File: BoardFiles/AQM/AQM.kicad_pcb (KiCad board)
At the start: 4 copper layers, 50.4 x 50.4 mm, 40 parts, among them J1 Conn_01x04, J2 Conn_01x04, J3 Conn_01x04, J4 Conn_01x04, J5 Conn_01x04, U1 KB2040

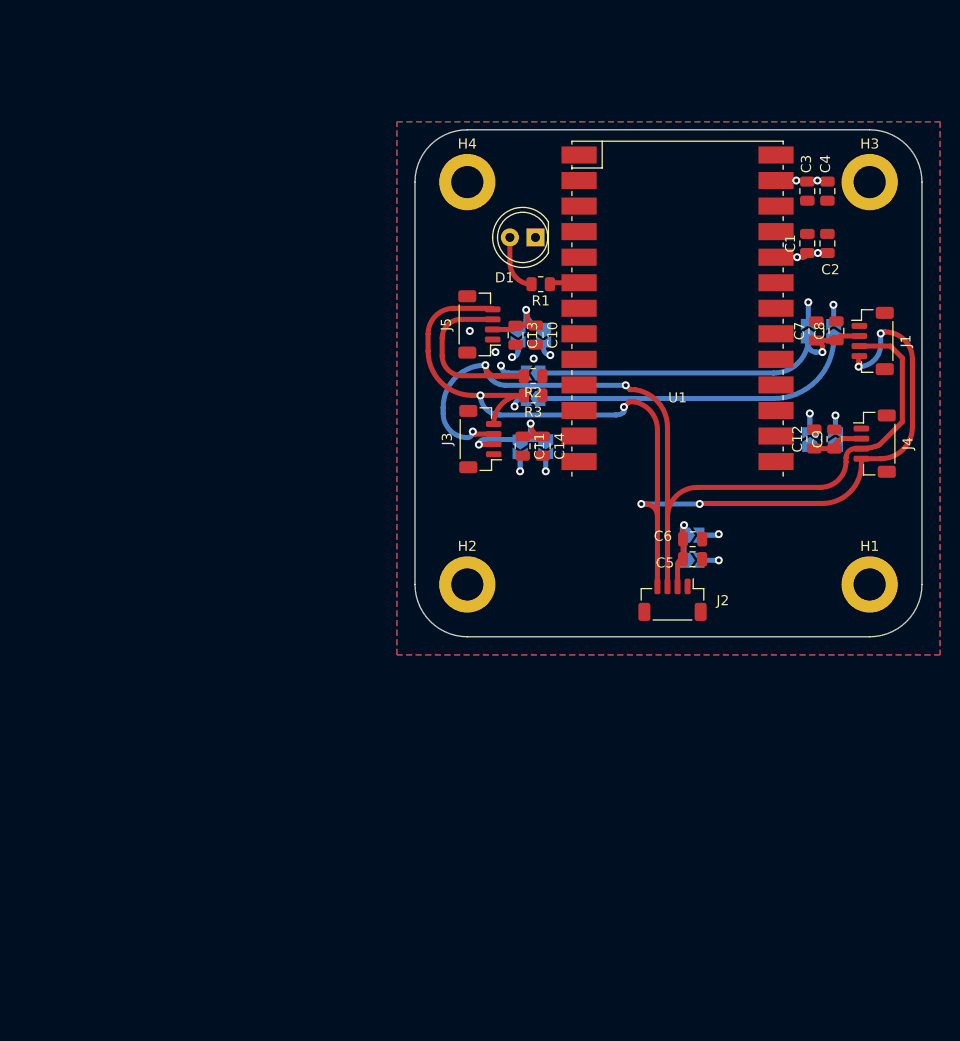
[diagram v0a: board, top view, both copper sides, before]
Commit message: Redid copper to make it look pretty
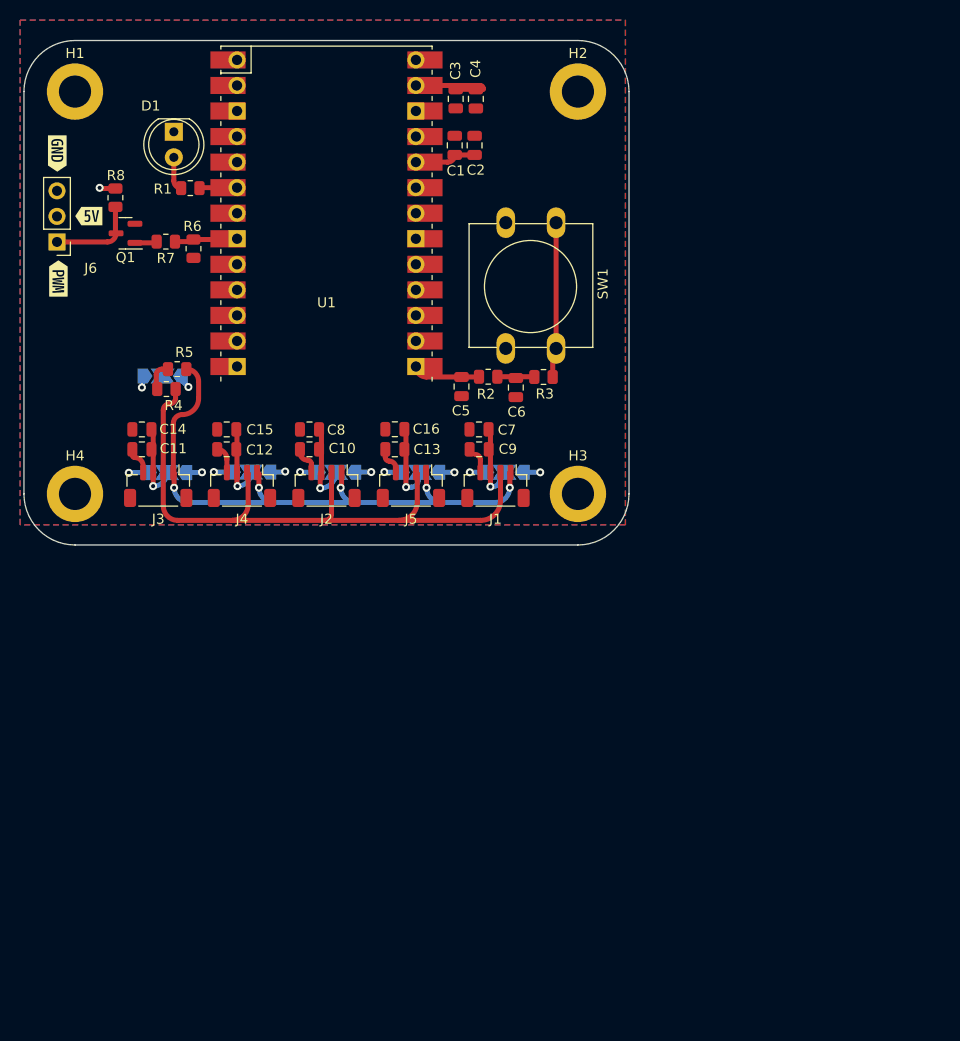
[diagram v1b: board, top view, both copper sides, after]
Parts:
- removed JP10, JP11, JP12, JP7, JP8, JP9: Jumper_2_Open, Jumper:SolderJumper-2_P1.3mm_Open_TrianglePad1.0x1.5mm
- added C15: 10u, Capacitor_SMD:C_0805_2012Metric, F.Cu at (110.1, 78.6)
- added C16: 10u, Capacitor_SMD:C_0805_2012Metric, F.Cu at (126.8, 78.6)
- added J6: Conn_01x03, Connector_PinHeader_2.54mm:PinHeader_1x03_P2.54mm_Vertical, F.Cu at (93.2, 60.0)
- added Q1: BSS138, Package_TO_SOT_SMD:SOT-23, F.Cu at (100.0, 59.1)
- added R4: 4.7K, Resistor_SMD:R_0805_2012Metric, F.Cu at (104.1, 74.6)
- added R5: 4.7K, Resistor_SMD:R_0805_2012Metric, F.Cu at (105.2, 72.6)
- added R6: 1k, Resistor_SMD:R_0805_2012Metric, F.Cu at (106.8, 60.6)
- added R7: 1k, Resistor_SMD:R_0805_2012Metric, F.Cu at (104.0, 59.9)
- added R8: 1k, Resistor_SMD:R_0805_2012Metric, F.Cu at (99.0, 55.5)
- added SW1: SW_Push, Button_Switch_THT:SW_PUSH-12mm, F.Cu at (142.8, 58.0)
- added kibuzzard-6378EB76: G***, kibuzzard-6378EB76, B.Cu at (110.3, 85.7)
- added kibuzzard-6378EB76: G***, kibuzzard-6378EB76, B.Cu at (127.1, 85.7)
- added kibuzzard-6378EB76: G***, kibuzzard-6378EB76, B.Cu at (118.7, 85.8)
- added kibuzzard-6378EB76: G***, kibuzzard-6378EB76, B.Cu at (102.0, 85.8)
- added kibuzzard-6378EB76: G***, kibuzzard-6378EB76, B.Cu at (135.4, 85.8)
- added kibuzzard-6378EBEC: G***, kibuzzard-6378EBEC, B.Cu at (139.7, 85.8)
- added kibuzzard-6378EBEC: G***, kibuzzard-6378EBEC, B.Cu at (114.6, 85.7)
- added kibuzzard-6378EBEC: G***, kibuzzard-6378EBEC, B.Cu at (122.9, 85.7)
- added kibuzzard-6378EBEC: G***, kibuzzard-6378EBEC, B.Cu at (131.4, 85.7)
- added kibuzzard-6378EBEC: G***, kibuzzard-6378EBEC, B.Cu at (106.1, 85.7)
- added kibuzzard-6378ECA4: G***, kibuzzard-6378ECA4, B.Cu at (101.5, 70.3)
- added kibuzzard-6378F2C3: G***, kibuzzard-6378F2C3, F.Cu at (93.3, 63.6)
- added kibuzzard-6378F2ED: G***, kibuzzard-6378F2ED, F.Cu at (93.2, 51.2)
- added kibuzzard-6378F316: G***, kibuzzard-6378F316, F.Cu at (96.4, 57.4)
- added kibuzzard-6378F9DB: G***, kibuzzard-6378F9DB, B.Cu at (105.6, 70.3)
- C12, C13, C6: value 10u -> 1u
- C7: value 1u -> 10u
- JP1, JP2, JP3, JP4, JP5, JP6: value Jumper_2_Open -> SolderJumper_3_Open; footprint Jumper:SolderJumper-2_P1.3mm_Open_TrianglePad1.0x1.5mm -> Jumper:SolderJumper-3_P2.0mm_Open_TrianglePad1.0x1.5mm_NumberLabels
- R2, R3: value 4.7K -> 10k
- moved H1 93.0 mm to (95.0, 45.0)
- moved J4 63.0 mm to (111.6, 84.2), turned to 180 degrees
- moved C12 58.4 mm to (110.1, 80.6), turned to 180 degrees
- moved JP3 55.0 mm to (103.7, 73.3), turned to 180 degrees
- moved C8 53.3 mm to (118.3, 78.6), turned to 180 degrees
- moved JP4 52.9 mm to (104.2, 82.9)
- moved H2 50.2 mm to (145.0, 45.0)
- moved H4 49.8 mm to (95.0, 85.0)
- moved H3 42.4 mm to (145.0, 85.0)
- moved J1 40.2 mm to (136.8, 84.2), turned to 180 degrees
- moved C14 39.9 mm to (101.7, 78.6), turned to 180 degrees
- moved C11 37.9 mm to (101.7, 80.6), turned to 180 degrees
- moved D1 37.5 mm to (104.8, 49.0), turned to -90 degrees
- moved C2 36.4 mm to (134.7, 50.4)
- moved C1 36.4 mm to (132.8, 50.4)
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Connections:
- C13 pad 1: Net-(C10-Pad1) -> Net-(C13-Pad1)
- C5 pad 1: Net-(C5-Pad1) -> Net-(U1-Pad14)
- C6 pad 1: Net-(C5-Pad1) -> Net-(C6-Pad1)
- C8 pad 1: Net-(C7-Pad1) -> Net-(C10-Pad1)
- C9 pad 1: Net-(C12-Pad1) -> Net-(C7-Pad1)
- J1 pad 1: GND -> /I2C/I2C.SCL
- J1 pad 2: Net-(C7-Pad1) -> /I2C/I2C.SDA
- J1 pad 3: /I2C.SDA -> Net-(C7-Pad1)
- J1 pad 4: /I2C.SCL -> GND
- J2 pad 1: GND -> /I2C/I2C.SCL
- J2 pad 2: Net-(C5-Pad1) -> /I2C/I2C.SDA
- J2 pad 3: /I2C.SDA -> Net-(C10-Pad1)
- J2 pad 4: /I2C.SCL -> GND
- J3 pad 1: GND -> /I2C/I2C.SCL
- J3 pad 2: Net-(C11-Pad1) -> /I2C/I2C.SDA
- J3 pad 3: /I2C.SDA -> Net-(C11-Pad1)
- J3 pad 4: /I2C.SCL -> GND
- J4 pad 1: GND -> /I2C/I2C.SCL
- J4 pad 2: Net-(C12-Pad1) -> /I2C/I2C.SDA
- J4 pad 3: /I2C.SDA -> Net-(C12-Pad1)
- J4 pad 4: /I2C.SCL -> GND
- J5 pad 1: GND -> /I2C/I2C.SCL
- J5 pad 2: Net-(C10-Pad1) -> /I2C/I2C.SDA
- J5 pad 3: /I2C.SDA -> Net-(C13-Pad1)
- J5 pad 4: /I2C.SCL -> GND
- JP1 pad 1: Net-(JP1-Pad1) -> +3V3
- JP1 pad 2: +3V3 -> Net-(C7-Pad1)
- JP2 pad 1: Net-(JP1-Pad1) -> +3V3
- JP2 pad 2: VBUS -> Net-(C10-Pad1)
- JP3 pad 1: Net-(C5-Pad1) -> +3V3
- JP3 pad 2: +3V3 -> Net-(R4-Pad1)
- JP4 pad 1: Net-(C5-Pad1) -> +3V3
- JP4 pad 2: VBUS -> Net-(C11-Pad1)
- JP5 pad 1: Net-(C7-Pad1) -> +3V3
- JP5 pad 2: +3V3 -> Net-(C12-Pad1)
- JP6 pad 1: Net-(C10-Pad1) -> +3V3
- JP6 pad 2: +3V3 -> Net-(C13-Pad1)
- R2 pad 1: Net-(JP1-Pad1) -> Net-(U1-Pad14)
- R2 pad 2: /I2C.SDA -> Net-(C6-Pad1)
- R3 pad 1: Net-(JP1-Pad1) -> Net-(C6-Pad1)
- R3 pad 2: /I2C.SCL -> Net-(R3-Pad2)
- U1 pad 14: unconnected-(U1-Pad14) -> Net-(U1-Pad14)
- U1 pad 8: unconnected-(U1-Pad8) -> Net-(U1-Pad8)
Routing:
- net /I2C.SCL: track 112.9 -> 0.00 mm, vias 6 -> 0
- net /I2C.SDA: track 111.7 -> 0.00 mm, vias 3 -> 0
- net /I2C/I2C.SDA: track 0.00 -> 66.9 mm
- net /I2C/I2C.SCL: track 0.00 -> 61.7 mm, vias 0 -> 5
- net Net-(JP1-Pad1): track 32.3 -> 0.00 mm
- net Net-(C7-Pad1): track 36.8 -> 7.06 mm
- net Net-(R3-Pad2): track 0.00 -> 15.5 mm
- net GND: track 0.14 -> 13.5 mm, vias 3 -> 0
- net Net-(C5-Pad1): track 9.98 -> 0.00 mm, vias 1 -> 0
- net Net-(J6-Pad1): track 0.00 -> 8.99 mm
- net Net-(C13-Pad1): track 0.00 -> 7.44 mm, vias 0 -> 1
- net Net-(U1-Pad14): track 0.00 -> 6.84 mm
- net Net-(C11-Pad1): track 14.5 -> 7.83 mm, vias 2 -> 1
- net Net-(U1-Pad8): track 0.00 -> 6.32 mm
- net Net-(C6-Pad1): track 0.00 -> 3.69 mm
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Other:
- board size 50.4 x 50.4 mm -> 60.1 x 50.2 mm
- board text added: "I2C PULL-UP"
- board text added: "SENSOR POWER"

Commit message: Adding relative paths
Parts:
- removed D1: LED, LED_THT:LED_D5.0mm_Clear
- removed kibuzzard-6378F2C3: G***, kibuzzard-6378F2C3
- added C17: 1u, Capacitor_SMD:C_0805_2012Metric, F.Cu at (104.2, 70.0)
- added C18: 1u, Capacitor_SMD:C_0805_2012Metric, F.Cu at (104.2, 67.8)
- added J7: LED, Connector_PinSocket_2.54mm:PinSocket_1x02_P2.54mm_Vertical, F.Cu at (104.9, 51.4)
- added J8: USER BUTTON, Connector_PinSocket_2.54mm:PinSocket_1x02_P2.54mm_Vertical, F.Cu at (103.5, 64.6)
- added R10: 10k, Resistor_SMD:R_0805_2012Metric, F.Cu at (107.0, 65.8)
- added R9: 10k, Resistor_SMD:R_0805_2012Metric, F.Cu at (107.0, 69.3)
- added kibuzzard-637AF59B: G***, kibuzzard-637AF59B, F.Cu at (95.3, 64.8)
- added kibuzzard-637AF633: G***, kibuzzard-637AF633, F.Cu at (96.9, 60.8)
- added kibuzzard-637AF646: G***, kibuzzard-637AF646, F.Cu at (102.1, 50.3)
- moved R8 2.22 mm to (96.9, 54.9), turned to 180 degrees
- moved Q1 0.38 mm to (100.4, 59.1)
- moved R7 0.07 mm to (104.1, 59.9)
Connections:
- J6 pad 1: Net-(J6-Pad1) -> Net-(U1-Pad7)
- J6 pad 3: GND -> Net-(R8-Pad2)
- Q1 pad 3: Net-(J6-Pad1) -> Net-(Q1-Pad3)
- R8 pad 1: Net-(J6-Pad1) -> Net-(Q1-Pad3)
- R8 pad 2: VBUS -> Net-(R8-Pad2)
- U1 pad 13: unconnected-(U1-Pad13) -> Net-(U1-Pad13)
- U1 pad 7: unconnected-(U1-Pad7) -> Net-(U1-Pad7)
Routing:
- net Net-(U1-Pad7): track 0.00 -> 19.4 mm, vias 0 -> 1
- net Net-(J6-Pad1): track 8.99 -> 0.00 mm
- net Net-(U1-Pad13): track 0.00 -> 7.17 mm
- net Net-(Q1-Pad3): track 0.00 -> 5.08 mm
- net Net-(J8-Pad1): track 0.00 -> 3.69 mm
- net Net-(C18-Pad1): track 0.00 -> 3.60 mm
- net Net-(R8-Pad2): track 0.00 -> 2.79 mm
- net VBUS: track 19.8 -> 18.2 mm, vias 7 -> 6

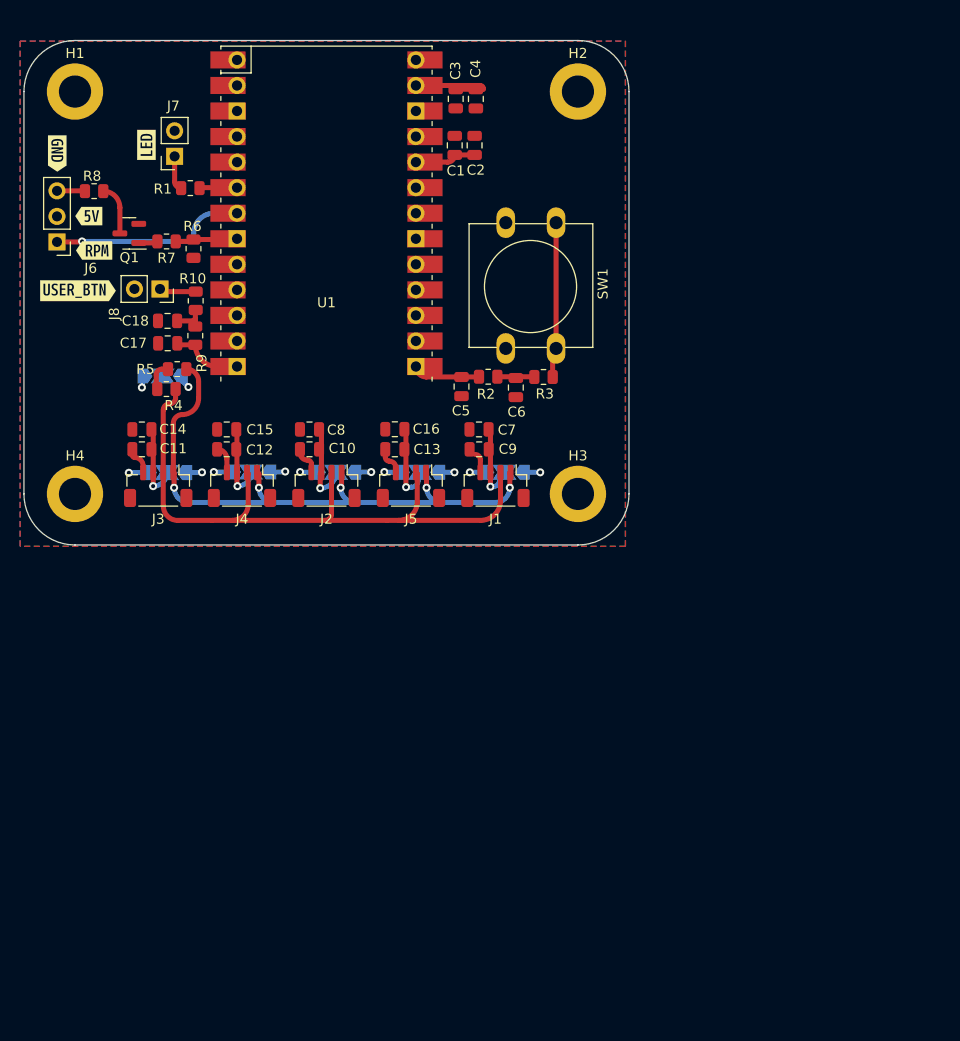
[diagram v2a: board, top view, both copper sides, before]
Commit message: Generating drawings and gerbers
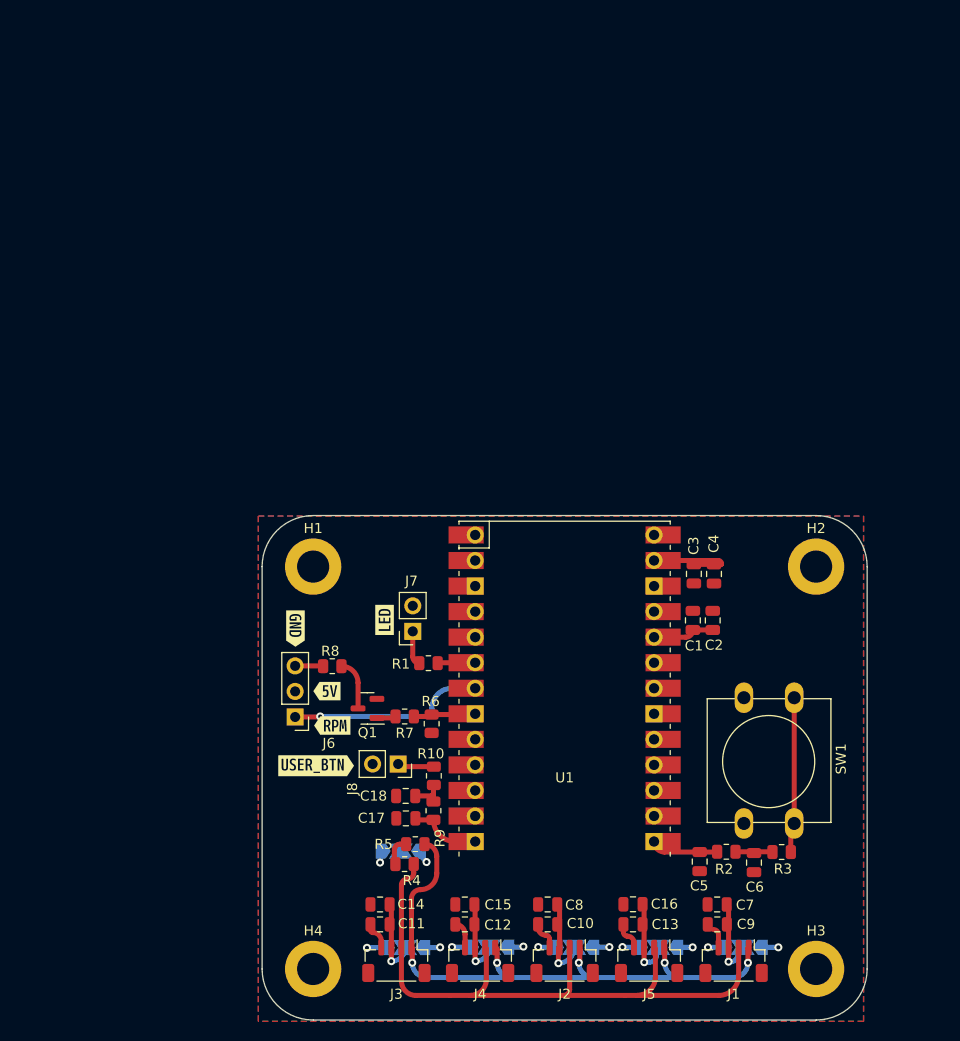
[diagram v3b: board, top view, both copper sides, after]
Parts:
- moved C10 52.8 mm to (142.0, 127.8)
- moved C11 52.8 mm to (125.3, 127.8)
- moved C12 52.8 mm to (133.8, 127.8)
- moved C13 52.8 mm to (150.5, 127.8)
- moved C14 52.8 mm to (125.3, 125.8)
- moved C15 52.8 mm to (133.8, 125.8)
- moved C16 52.8 mm to (150.5, 125.8)
- moved C18 52.8 mm to (127.9, 115.0)
- moved C6 52.8 mm to (162.5, 121.7)
- moved C7 52.8 mm to (158.8, 125.8)
- moved C8 52.8 mm to (142.0, 125.8)
- moved C9 52.8 mm to (158.9, 127.8)
- moved J2 52.8 mm to (143.7, 131.4)
- moved J3 52.8 mm to (127.0, 131.4)
- moved J4 52.8 mm to (135.3, 131.4)
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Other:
- board size 60.1 x 50.2 mm -> 60.2 x 50.2 mm
- board text added: "1. BOARD FILES CAN BE FOUND ON https://github.com/warlock31415/AQM"
- board text added: "ASSEMBLY NOTES:"
